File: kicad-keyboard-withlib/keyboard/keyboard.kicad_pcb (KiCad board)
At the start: 2 copper layers, 200.5 x 128.5 mm, 45 parts, among them SW1 SW_Push, SW10 SW_Push, SW11 SW_Push, SW12 SW_Push, SW13 SW_Push, SW14 SW_Push, SW15 SW_Push, SW16 SW_Push, SW17 SW_Push, SW18 SW_Push, SW19 SW_Push, SW2 SW_Push, SW20 SW_Push, SW21 SW_Push, SW22 SW_Push, SW23 SW_Push, SW24 SW_Push, SW25 SW_Push, SW26 SW_Push, SW27 SW_Push, SW28 SW_Push, SW29 SW_Push, SW3 SW_Push, SW30 SW_Push, SW31 SW_Push, SW32 SW_Push, SW33 SW_Push, SW34 SW_Push, SW35 SW_Push, SW36 SW_Push, SW37 SW_Push, SW38 SW_Push, SW39 SW_Slide_DPDT, SW4 SW_Push, SW41 RotaryEncoder_Switch, SW5 SW_Push, SW6 SW_Push, SW7 SW_Push, SW8 SW_Push, SW9 SW_Push, U2 MCP23017_SO

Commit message: clean pcb with good i2c footprint
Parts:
- added D1: LED, LED_SMD:LED_0603_1608Metric_Pad1.05x0.95mm_HandSolder, F.Cu at (145.6, 43.5)
- added R4: 10K, Resistor_SMD:R_0603_1608Metric_Pad0.98x0.95mm_HandSolder, F.Cu at (145.6, 47.5)
- R1, R2, R3: value R -> Heater
- U2: footprint Package_SO:SOIC-28W_7.5x17.9mm_P1.27mm -> Package_SO:SSOP-28_5.3x10.2mm_P0.65mm
- moved R3 6.10 mm to (203.5, 70.0)
- moved R2 6.10 mm to (199.5, 65.1), turned to -90 degrees
- moved R1 5.06 mm to (216.2, 71.0)
- moved U2 2.76 mm to (219.2, 59.7)
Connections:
- net /GND renamed GND
- P1 pad 16: Net-(P1-VCC) -> VCC
- R1 pad 1: Net-(P1-VCC) -> VCC
- R2 pad 1: Net-(P1-VCC) -> VCC
- R2 pad 2: Net-(P1-SDA) -> Net-(P1-SCL)
- R3 pad 1: Net-(P1-SCL) -> VCC
- R3 pad 2: Net-(P1-VCC) -> Net-(P1-SDA)
- U2 pad 9: Net-(P1-VCC) -> VCC
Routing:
- net VCC: track 0.00 -> 186.5 mm
- net Net-(P1-VCC): track 183.0 -> 0.00 mm
- net Net-(P1-SDA): track 142.6 -> 150.0 mm
- net Net-(P1-SCL): track 138.7 -> 145.5 mm
- net Net-(D1-K): track 0.00 -> 4.03 mm
- net Net-(U2-~{RESET}): track 12.0 -> 13.8 mm
- net Net-(U2-GPA7): track 38.5 -> 39.4 mm
- net Net-(U2-GPA6): track 40.6 -> 41.3 mm
- net GND: track 9.77 -> 10.3 mm, vias 4 -> 5

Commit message: more footprint, started to replace in the pcb
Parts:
- D1: footprint LED_SMD:LED_0603_1608Metric_Pad1.05x0.95mm_HandSolder -> Lilyspad:led
- R1: value Heater -> 10K; footprint Resistor_SMD:R_0603_1608Metric_Pad0.98x0.95mm_HandSolder -> Lilyspad:Resistance
- R2, R3: value Heater -> 4.7K; footprint Resistor_SMD:R_0603_1608Metric_Pad0.98x0.95mm_HandSolder -> Lilyspad:Resistance
- R4: footprint Resistor_SMD:R_0603_1608Metric_Pad0.98x0.95mm_HandSolder -> Lilyspad:Resistance
- U2: footprint Package_SO:SSOP-28_5.3x10.2mm_P0.65mm -> Lilyspad:MCP23017
- moved U2 6.80 mm to (212.9, 57.2)
- moved R3 4.47 mm to (199.1, 69.0)
- moved R1 4.00 mm to (213.2, 68.5)
- moved D1 2.22 mm to (145.6, 41.3)
- moved R2 1.90 mm to (201.4, 65.1)
- moved R4 1.85 mm to (145.6, 45.7)
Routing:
- net Net-(P1-SDA): track 150.0 -> 138.0 mm
- net VCC: track 186.5 -> 174.6 mm
- net Net-(P1-SCL): track 145.5 -> 134.2 mm
- net Net-(U2-GPA6): track 41.3 -> 49.3 mm
- net Net-(U2-GPA7): track 39.4 -> 35.1 mm
- net Net-(U2-~{RESET}): track 13.8 -> 11.3 mm
- net GND: track 10.3 -> 12.4 mm
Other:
- board text removed: "10K"
- board text removed: "4,7K"

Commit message: add: footprint for slide switch and added it to pcb
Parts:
- SW39: footprint Button_Switch_THT:SW_CK_JS202011CQN_DPDT_Straight -> Lilyspad:slide_switch
- moved SW39 5.59 mm to (147.0, 51.2)
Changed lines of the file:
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@@
 		)
 	)
-	(footprint "Button_Switch_THT:SW_CK_JS202011CQN_DPDT_Straight"
+	(footprint "Lilyspad:slide_switch"
 		(layer "F.Cu")
-		(at 144.5 56.2)
-		(descr "C&K sub miniature slide switch, JS series, DPDT, right angle, http://www.ckswitches.com/media/1422/js.pdf")
-		(tags "switch DPDT")
+		(at 147 51.2)
 		(property "Reference" "SW39"
-			(at 2.75 -1.6 0)
-			(layer "F.SilkS")
-			(effects
-				(font
-					(size 1 1)
-					(thickness 0.15)
+			(at 0 -0.5 0)
+			(unlocked yes)
+			(layer "F.SilkS")
+			(effects
+				(font
+					(size 1 1)
+					(thickness 0.1)
 				)
 			)
 		)
 		(property "Value" "SW_Slide_DPDT"
-			(at 3 5 0)
+			(at 0 1 0)
+			(unlocked yes)
 			(layer "F.Fab")
 			(effects
@@
 			(effects
 				(font
-					(size 1.27 1.27)
+					(size 1 1)
 					(thickness 0.15)
 				)
@@
 			(effects
 				(font
-					(size 1.27 1.27)
+					(size 1 1)
 					(thickness 0.15)
 				)
@@
 		(sheetname "/")
 		(sheetfile "keyboard.kicad_sch")
-		(attr through_hole)
-		(fp_line
-			(start -2.1 -0.45)
-			(end -2.1 3.75)
-			(stroke
-				(width 0.12)
-				(type solid)
-			)
-			(layer "F.SilkS")
-		)
-		(fp_line
-			(start -2.1 3.75)
-			(end -0.9 3.75)
-			(stroke
-				(width 0.12)
-				(type solid)
-			)
-			(layer "F.SilkS")
-		)
-		(fp_line
-			(start -1.75 -0.45)
-			(end -2.1 -0.45)
-			(stroke
-				(width 0.12)
-				(type solid)
-			)
-			(layer "F.SilkS")
-		)
-		(fp_line
-			(start 5.9 -0.45)
-			(end 7.1 -0.45)
-			(stroke
-				(width 0.12)
-				(type solid)
-			)
-			(layer "F.SilkS")
-		)
-		(fp_line
-			(start 7.1 -0.45)
-			(end 7.1 3.75)
-			(stroke
-				(width 0.12)
-				(type solid)
-			)
-			(layer "F.SilkS")
-		)
-		(fp_line
-			(start 7.1 3.75)
-			(end 5.9 3.75)
-			(stroke
-				(width 0.12)
-				(type solid)
-			)
-			(layer "F.SilkS")
-		)
-		(fp_poly
-			(pts
-				(xy -1 -0.45) (xy -1.48 -0.45) (xy -1 -0.93) (xy -1 -0.45)
-			)
-			(stroke
-				(width 0.12)
-				(type solid)
-			)
-			(fill yes)
-			(layer "F.SilkS")
-		)
-		(fp_line
-			(start -2.25 -0.95)
-			(end 7.25 -0.95)
+		(attr smd)
+		(fp_line
+			(start -3.5 4)
+			(end -3.5 5)
+			(stroke
+				(width 0.1)
+				(type default)
+			)
+			(layer "F.SilkS")
+		)
+		(fp_line
+			(start -2.5 4)
+			(end -3.5 4)
+			(stroke
+				(width 0.1)
+				(type default)
+			)
+			(layer "F.SilkS")
+		)
+		(fp_line
+			(start -1.5 4)
+			(end 3 4)
+			(stroke
+				(width 0.1)
+				(type default)
+			)
+			(layer "F.SilkS")
+		)
+		(fp_line
+			(start 0.49 6.2)
+			(end 0.49 7.2)
+			(stroke
+				(width 0.1)
+				(type default)
+			)
+			(layer "F.SilkS")
+		)
+		(fp_line
+			(start 0.49 7.2)
+			(end 1.99 7.2)
+			(stroke
+				(width 0.1)
+				(type default)
+			)
+			(layer "F.SilkS")
+		)
+		(fp_line
+			(start 1.99 6.2)
+			(end 0.49 6.2)
+			(stroke
+				(width 0.1)
+				(type default)
+			)
+			(layer "F.SilkS")
+		)
+		(fp_line
+			(start 1.99 7.2)
+			(end 1.99 6.2)
+			(stroke
+				(width 0.1)
+				(type default)
+			)
+			(layer "F.SilkS")
+		)
+		(fp_line
+			(start 3 9.5)
+			(end -1.5 9.5)
+			(stroke
+				(width 0.1)
+				(type default)
+			)
+			(layer "F.SilkS")
+		)
+		(fp_line
+			(start 3.5 4.5)
+			(end 3.5 8.5)
+			(stroke
+				(width 0.1)
+				(type default)
+			)
+			(layer "F.SilkS")
+		)
+		(fp_rect
+			(start -4 3.5)
+			(end 4 10)
 			(stroke
 				(width 0.05)
-				(type solid)
-			)
+				(type default)
+			)
+			(fill no)
 			(layer "F.CrtYd")
 		)
-		(fp_line
-			(start -2.25 4.25)
-			(end -2.25 -0.95)
-			(stroke
-				(width 0.05)
-				(type solid)
-			)
-			(layer "F.CrtYd")
-		)
-		(fp_line
-			(start 7.25 -0.95)
-			(end 7.25 4.25)
-			(stroke
-				(width 0.05)
-				(type solid)
-			)
-			(layer "F.CrtYd")
-		)
-		(fp_line
-			(start 7.25 4.25)
-			(end -2.25 4.25)
-			(stroke
-				(width 0.05)
-				(type solid)
-			)
-			(layer "F.CrtYd")
-		)
-		(fp_line
-			(start -2 3.65)
-			(end -2 0.65)
-			(stroke
-				(width 0.1)
-				(type solid)
-			)
-			(layer "F.Fab")
-		)
-		(fp_line
-			(start -1 -0.35)
-			(end -2 0.65)
-			(stroke
-				(width 0.1)
-				(type solid)
-			)
-			(layer "F.Fab")
-		)
-		(fp_line
-			(start -1 -0.35)
-			(end 7 -0.35)
-			(stroke
-				(width 0.1)
-				(type solid)
-			)
-			(layer "F.Fab")
-		)
-		(fp_line
-			(start 7 -0.35)
-			(end 7 3.65)
-			(stroke
-				(width 0.1)
-				(type solid)
-			)
-			(layer "F.Fab")
-		)
-		(fp_line
-			(start 7 3.65)
-			(end -2 3.65)
-			(stroke
-				(width 0.1)
-				(type solid)
-			)
-			(layer "F.Fab")
-		)
 		(fp_text user "${REFERENCE}"
-			(at 2.5 1.65 0)
-			(layer "F.Fab")
-			(effects
-				(font
-					(size 1 1)
-					(thickness 0.15)
-				)
-			)
-		)
-		(pad "1" thru_hole roundrect
-			(at 0 0)
-			(size 1.4 1.4)
-			(drill 0.9)
-			(layers "*.Cu" "*.Mask")
-			(remove_unused_layers no)
-			(roundrect_rratio 0.1785714286)
+			(at 0 2.5 0)
+			(unlocked yes)
+			(layer "F.Fab")
+			(effects
+				(font
+					(size 1 1)
+					(thickness 0.15)
+				)
+			)
+		)
+		(pad "1" thru_hole rect
+			(at -2.5 5)
+			(size 1.52 1.52)
+			(drill 1.02)
+			(layers "*.Cu" "*.Mask")
+			(remove_unused_layers no)
 			(net 40 "Net-(P1-SLD_SW-Pad17)")
 			(pinfunction "A")
@@
 		)
 		(pad "2" thru_hole circle
-			(at 2.5 0)
-			(size 1.4 1.4)
-			(drill 0.9)
+			(at 0 5)
+			(size 1.52 1.52)
+			(drill 1.02)
 			(layers "*.Cu" "*.Mask")
 			(remove_unused_layers no)
@@
 		)
 		(pad "3" thru_hole circle
-			(at 5 0)
-			(size 1.4 1.4)
-			(drill 0.9)
+			(at 2.5 5)
+			(size 1.52 1.52)
+			(drill 1.02)
 			(layers "*.Cu" "*.Mask")
 			(remove_unused_layers no)
@@
 		)
 		(pad "4" thru_hole circle
-			(at 5 3.3)
-			(size 1.4 1.4)
-			(drill 0.9)
+			(at 2.5 8.4)
+			(size 1.52 1.52)
+			(drill 1.02)
 			(layers "*.Cu" "*.Mask")
 			(remove_unused_layers no)
@@
 		)
 		(pad "5" thru_hole circle
-			(at 2.5 3.3)
-			(size 1.4 1.4)
-			(drill 0.9)
+			(at 0 8.4)
+			(size 1.52 1.52)
+			(drill 1.02)
 			(layers "*.Cu" "*.Mask")
 			(remove_unused_layers no)
@@
 		)
 		(pad "6" thru_hole circle
-			(at 0 3.3)
-			(size 1.4 1.4)
-			(drill 0.9)
+			(at -2.5 8.4)
+			(size 1.52 1.52)
+			(drill 1.02)
 			(layers "*.Cu" "*.Mask")
 			(remove_unused_layers no)
@@
 		)
 		(embedded_fonts no)
-		(model "${KICAD9_3DMODEL_DIR}/Button_Switch_THT.3dshapes/SW_CK_JS202011CQN_DPDT_Straight.step"
-			(offset
-				(xyz 0 0 0)
-			)
-			(scale
-				(xyz 1 1 1)
-			)
-			(rotate
-				(xyz 0 0 0)
-			)
-		)
 	)
 	(footprint "Button_Switch_THT:SW_PUSH-12mm_Wuerth-430476085716"

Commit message: add: all footprint done, pcb with own footprint, to finish
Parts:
- removed SW41: RotaryEncoder_Switch, Rotary_Encoder:RotaryEncoder_Alps_EC11E-Switch_Vertical_H20mm
- added SW40: ~, Lilyspad:rotary_encoder, F.Cu at (177.8, 66.0)
- SW1, SW10, SW11, SW12, SW13, SW14, SW15, SW16, SW17, SW18, SW19, SW2, SW20, SW21, SW22, SW23, SW24, SW25, SW26, SW27, SW28, SW29, SW3, SW30, SW31, SW32, SW33, SW34, SW35, SW36, SW37, SW38, SW4, SW5, SW6, SW7, SW8, SW9: footprint Button_Switch_THT:SW_PUSH-12mm_Wuerth-430476085716 -> Lilyspad:push_switch
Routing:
- net Net-(P1-R3): track 412.2 -> 0.00 mm
- net Net-(P1-R4): track 410.5 -> 0.00 mm
- net Net-(P1-R2): track 386.5 -> 0.00 mm
- net Net-(P1-R1): track 355.4 -> 0.00 mm
- net Net-(P1-C8): track 235.9 -> 0.00 mm, vias 6 -> 0
- net Net-(P1-C10): track 200.5 -> 0.00 mm
- net Net-(P1-C7): track 186.2 -> 0.00 mm, vias 8 -> 0
- net Net-(P1-C9): track 182.6 -> 0.00 mm, vias 6 -> 0
- net Net-(P1-C6): track 171.6 -> 0.00 mm, vias 8 -> 0
- net Net-(P1-C5): track 156.3 -> 0.00 mm, vias 8 -> 0
- net Net-(P1-C4): track 141.4 -> 0.00 mm, vias 8 -> 0
- net Net-(P1-C3): track 132.5 -> 0.00 mm, vias 8 -> 0
- net Net-(P1-C2): track 127.2 -> 0.00 mm, vias 8 -> 0
- net Net-(P1-C1): track 126.4 -> 0.00 mm, vias 8 -> 0

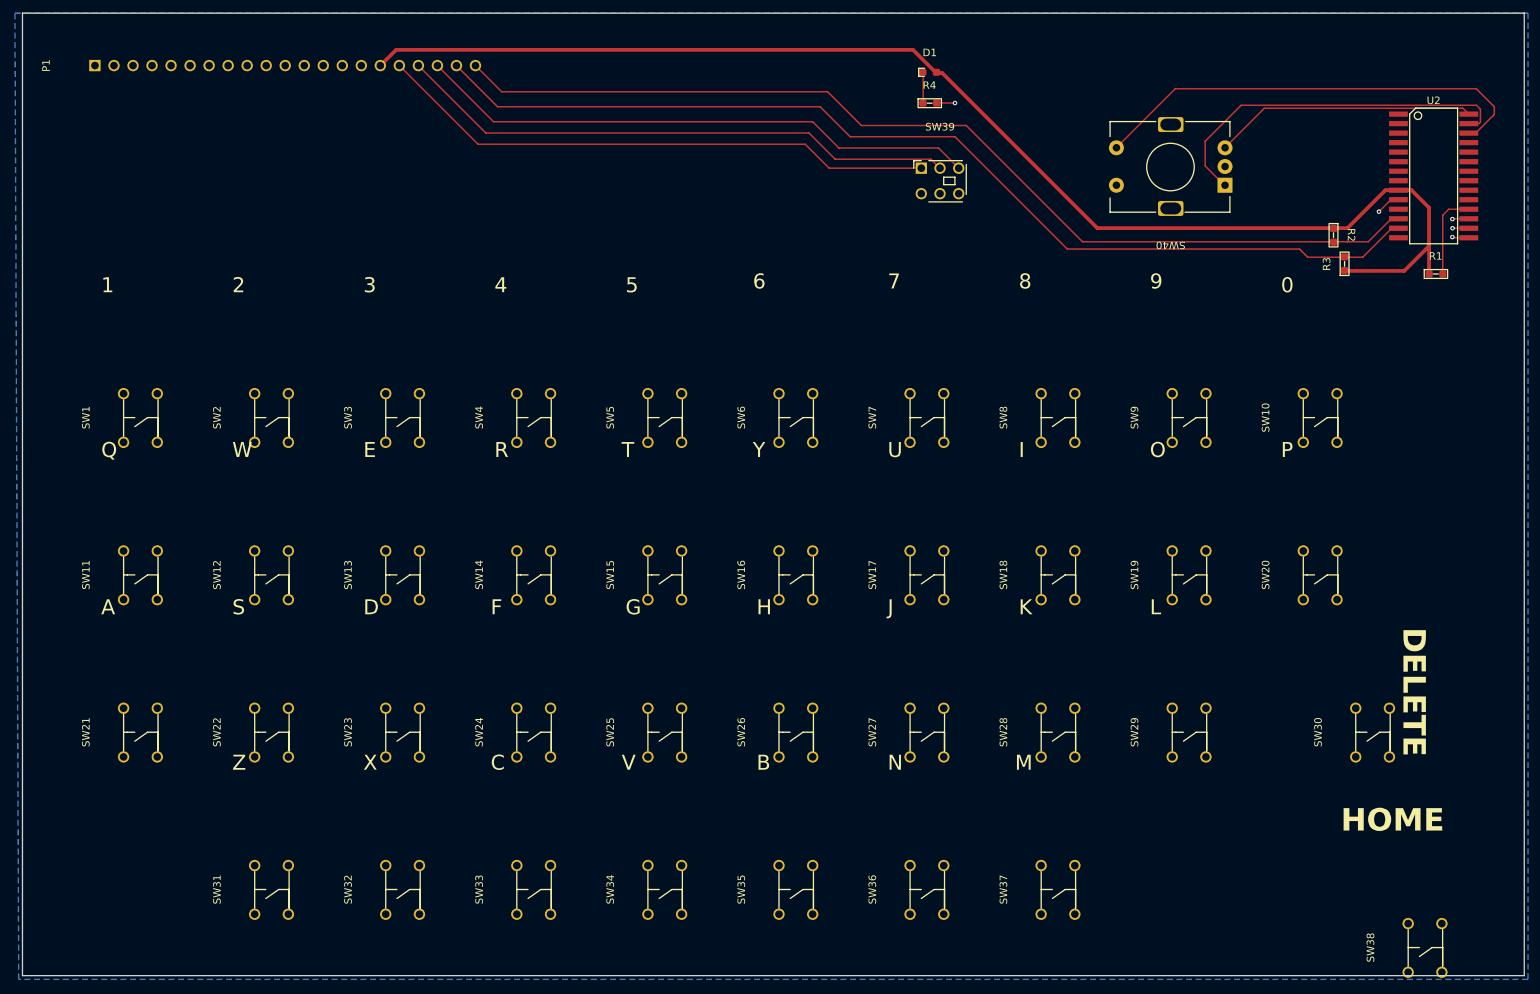
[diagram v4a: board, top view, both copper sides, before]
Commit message: setup v2 pcb keyboard, still an issue with the rotary, misses some symbole i think
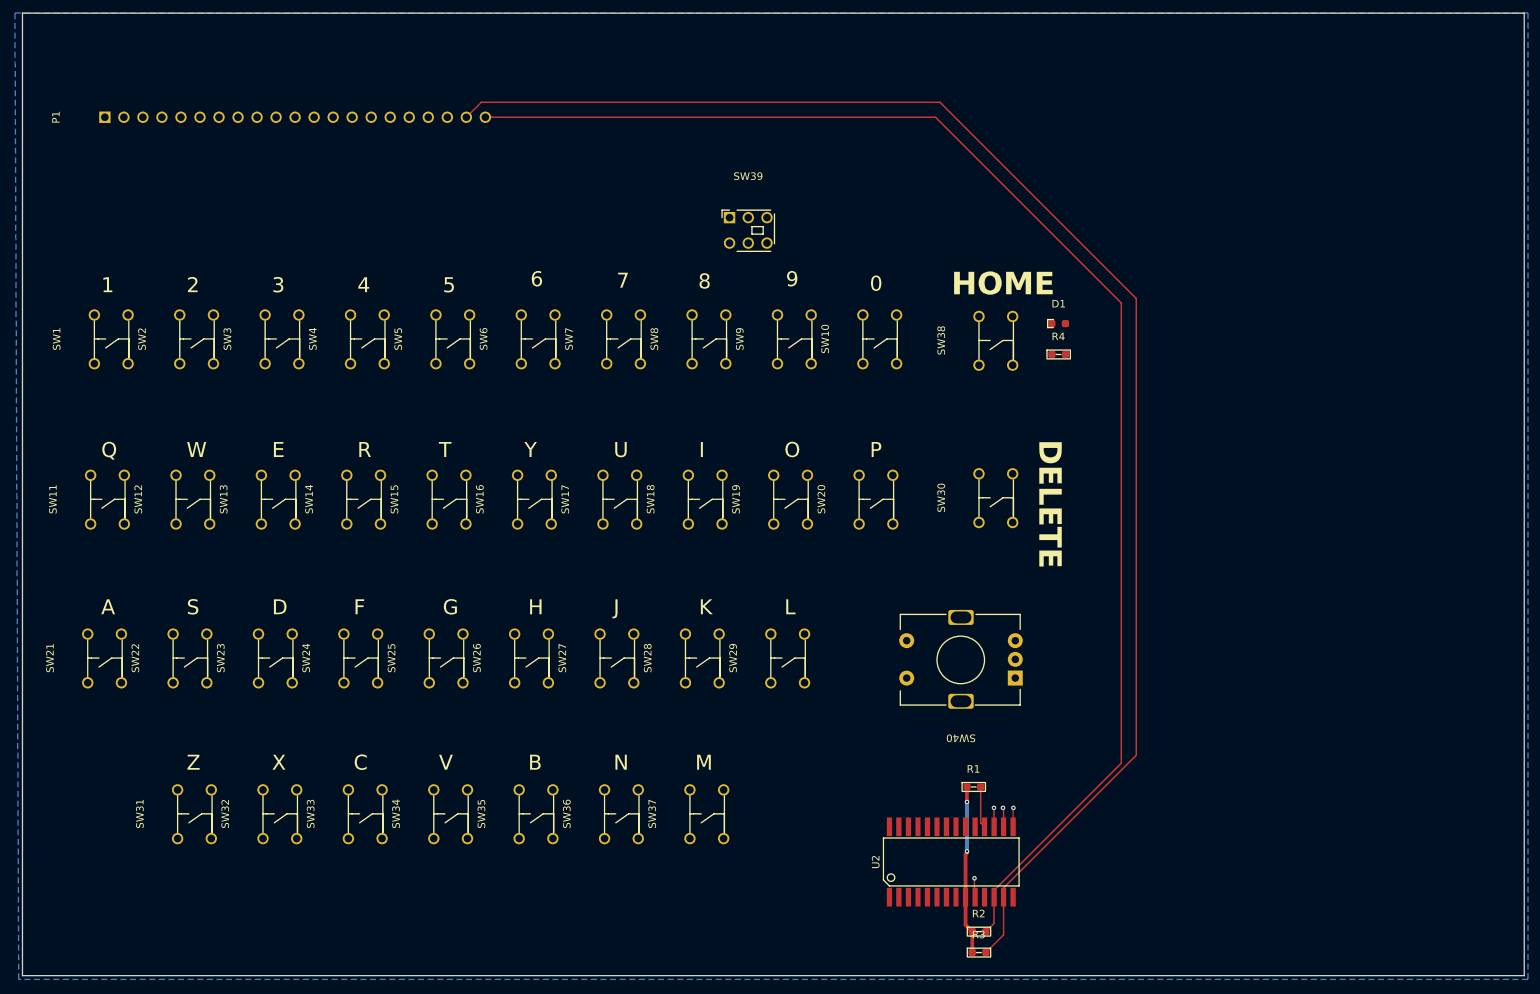
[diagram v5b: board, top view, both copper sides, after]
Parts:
- moved U2 112.0 mm to (148.5, 148.8), turned to 90 degrees
- moved R2 103.6 mm to (152.2, 156.3), turned to 0 degrees
- moved R3 101.6 mm to (152.2, 159.1), turned to 0 degrees
- moved SW38 99.3 mm to (147.7, 79.2)
- moved R1 92.2 mm to (151.5, 136.9)
- moved SW40 71.5 mm to (149.8, 131.8)
- moved SW20 60.2 mm to (131.7, 100.4)
- moved SW10 59.7 mm to (132.2, 79.0)
- moved SW30 59.2 mm to (147.7, 100.2)
- moved SW29 54.5 mm to (119.9, 121.6)
- moved SW19 54.2 mm to (120.3, 100.4)
- moved SW9 53.7 mm to (120.8, 79.0)
- moved SW28 48.5 mm to (108.5, 121.6)
- moved SW18 48.2 mm to (108.9, 100.4)
- moved SW37 48.0 mm to (109.1, 142.4)
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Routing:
- net VCC: track 174.6 -> 22.6 mm, vias 0 -> 2
- net Net-(P1-SLD_SW-Pad17): track 75.4 -> 0.00 mm
- net Net-(P1-SLD_SW-Pad18): track 75.3 -> 0.00 mm
- net Net-(P1-SLD_SW-Pad19): track 75.3 -> 0.00 mm
- net Net-(U2-GPA5): track 60.2 -> 0.00 mm
- net Net-(P1-SDA): track 138.0 -> 196.7 mm
- net Net-(P1-SCL): track 134.2 -> 186.6 mm
- net Net-(U2-GPA6): track 49.3 -> 0.00 mm
- net Net-(U2-GPA7): track 35.1 -> 0.00 mm
- net Net-(U2-~{RESET}): track 11.3 -> 5.54 mm
- net GND: track 12.4 -> 7.64 mm, vias 5 -> 4
- net Net-(D1-K): track 4.03 -> 0.11 mm
